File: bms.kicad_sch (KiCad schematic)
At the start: 62 parts, among them J1 Conn_01x13, U1 LMR51610, U2 STM32F103C8Tx, U3 MAX14920, U4 MAX11163, U5 MAX6126, Y1 8M

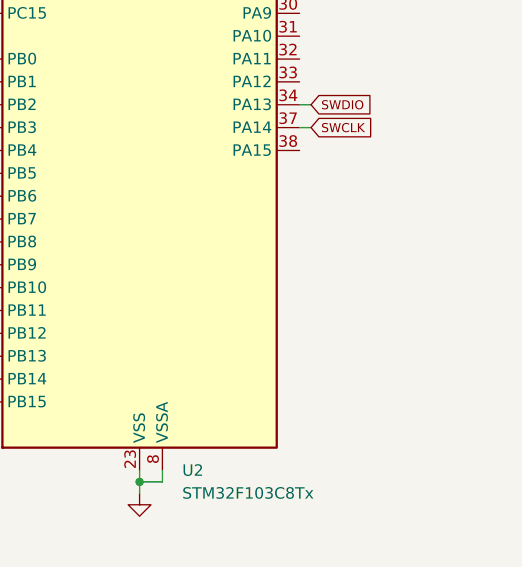
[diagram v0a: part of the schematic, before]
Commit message: schematic: Add SWD header
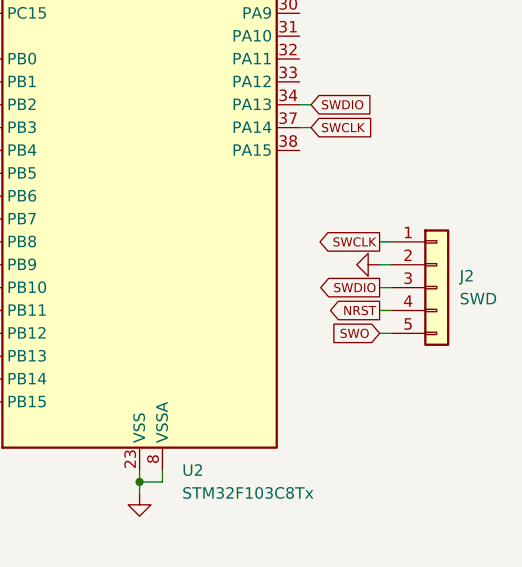
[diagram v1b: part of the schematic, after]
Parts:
- added J2: SWD, Connector_PinHeader_2.54mm:PinHeader_1x05_P2.54mm_Vertical, symbol Connector_Generic:Conn_01x05
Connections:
- net GND: now also J2.2 (Pin_2)
- net NRST: now also J2.4 (Pin_4)
- net SWCLK: now also J2.1 (Pin_1)
- net SWDIO: now also J2.3 (Pin_3)
- net SWO: now also J2.5 (Pin_5)

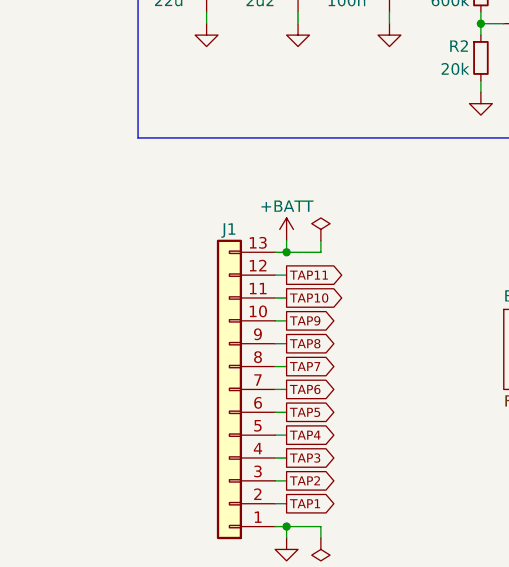
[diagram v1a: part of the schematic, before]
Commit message: schematic: Add mounting holes
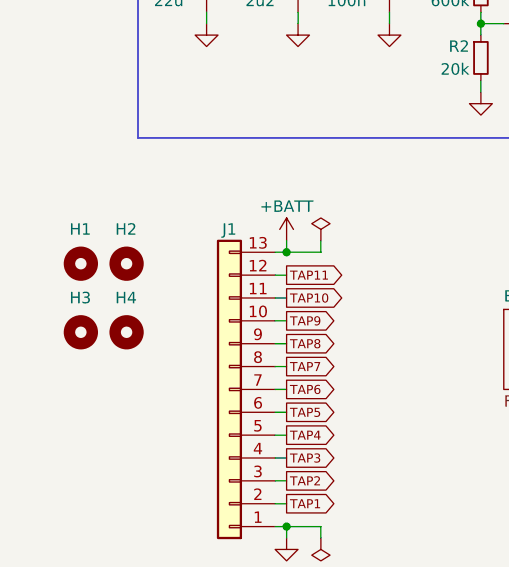
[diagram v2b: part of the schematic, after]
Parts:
- added H1, H2, H3, H4: MountingHole, MountingHole:MountingHole_3.2mm_M3, symbol Mechanical:MountingHole

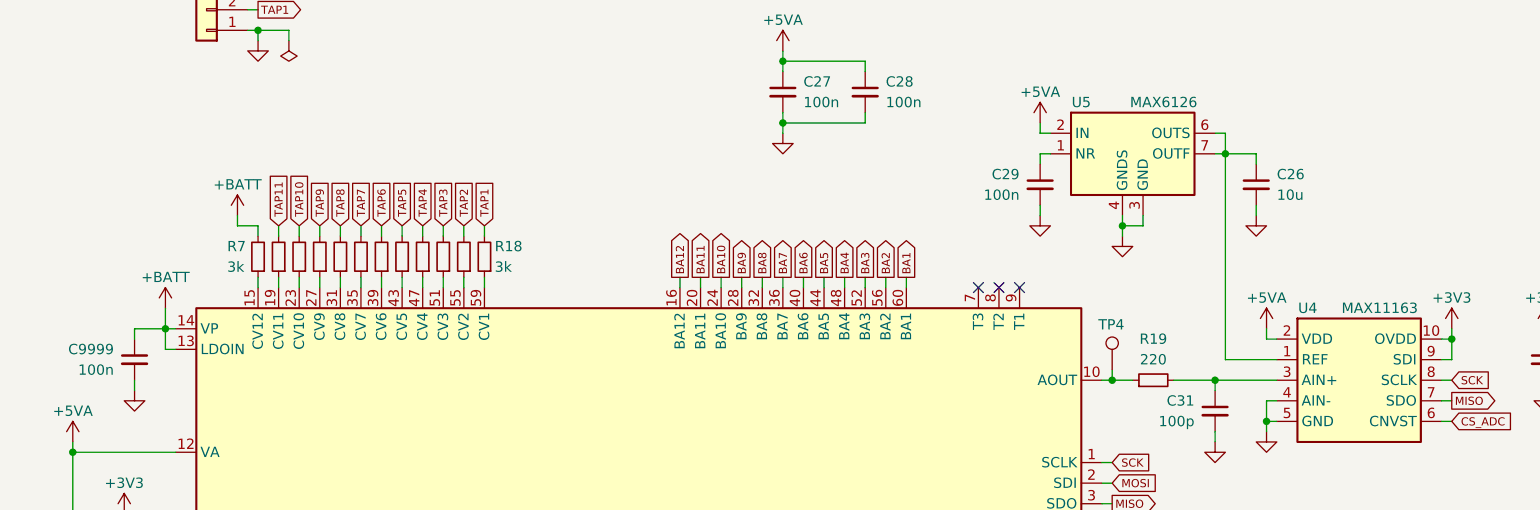
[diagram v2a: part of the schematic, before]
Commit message: schematic: Assign some more real components to passives
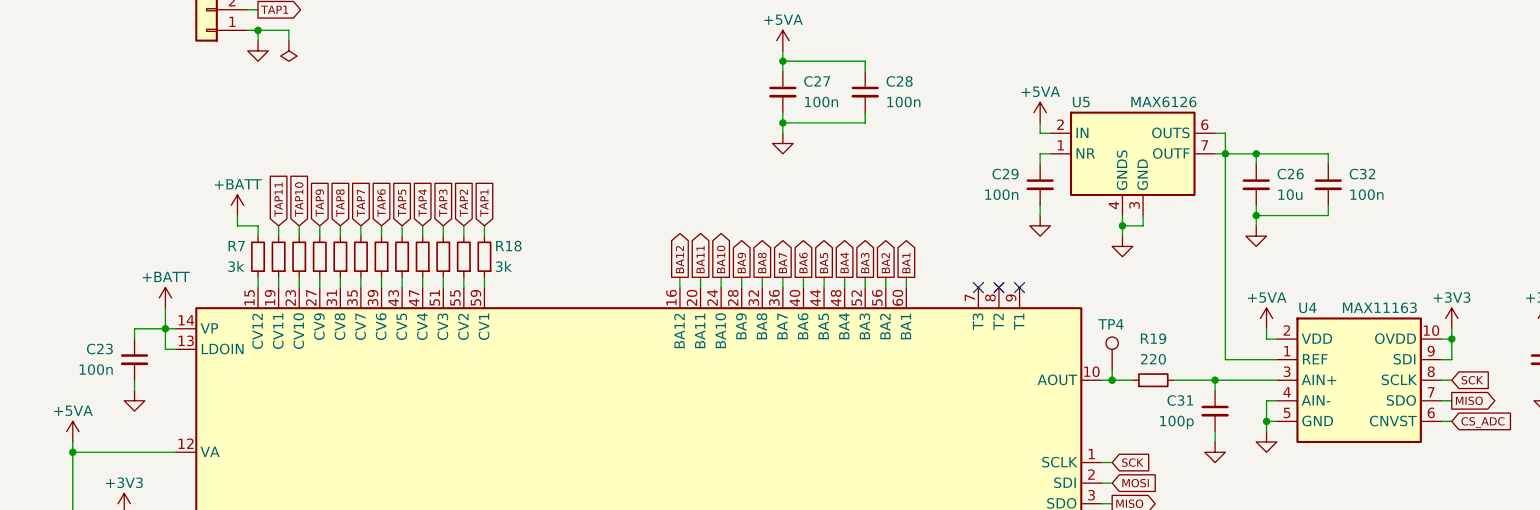
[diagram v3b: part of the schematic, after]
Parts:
- added C32: 100n, Capacitor_SMD:C_0603_1608Metric, symbol Device:C_Small
- C2: footprint (none) -> Capacitor_SMD:C_1210_3225Metric; Part Number (none) -> GRM32ER72A225KA35; Role (none) -> LMR51610 input decoupling
- C23: renamed from C9999; footprint (none) -> Capacitor_SMD:C_1206_3216Metric; Part Number (none) -> GRM31C5C2A104JA01L
- C26: footprint (none) -> Capacitor_SMD:C_1206_3216Metric; Part Number (none) -> GRM31CR71C106KA12L
- C3: footprint (none) -> Capacitor_SMD:C_1206_3216Metric; Part Number (none) -> GRM31C5C2A104JA01L; Role (none) -> LMR51610 input decoupling
- R10, R11, R12, R13, R14, R15, R16, R17, R18, R7, R8, R9: Part Number (none) -> 0603WAF3001T5E
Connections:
- net GND: now also C32.2
- net at C26.1, U4.1 (REF), U5.6 (OUTS)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: now also C32.1
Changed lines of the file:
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@@
 	)
 	(junction
+		(at 165.1 132.08)
+		(diameter 0)
+		(color 0 0 0 0)
+	)
+	(junction
 		(at 43.18 45.72)
 		(diameter 0)
@@
 	)
 	(junction
+		(at 165.1 124.46)
+		(diameter 0)
+		(color 0 0 0 0)
+	)
+	(junction
 		(at 33.02 45.72)
 		(diameter 0)
@@
 	(wire
 		(pts
+			(xy 173.99 125.73) (xy 173.99 124.46)
+		)
+		(stroke
+			(width 0)
+			(type default)
+		)
+	)
+	(wire
+		(pts
 			(xy 224.79 87.63) (xy 226.06 87.63)
 		)
@@
 	(wire
 		(pts
+			(xy 173.99 130.81) (xy 173.99 132.08)
+		)
+		(stroke
+			(width 0)
+			(type default)
+		)
+	)
+	(wire
+		(pts
 			(xy 138.43 121.92) (xy 139.7 121.92)
 		)
@@
 	(wire
 		(pts
+			(xy 165.1 132.08) (xy 173.99 132.08)
+		)
+		(stroke
+			(width 0)
+			(type default)
+		)
+	)
+	(wire
+		(pts
 			(xy 224.79 39.37) (xy 226.06 39.37)
 		)
@@
 	(wire
 		(pts
+			(xy 165.1 132.08) (xy 165.1 133.35)
+		)
+		(stroke
+			(width 0)
+			(type default)
+		)
+	)
+	(wire
+		(pts
 			(xy 41.91 109.22) (xy 41.91 110.49)
 		)
@@
 	(wire
 		(pts
+			(xy 173.99 124.46) (xy 165.1 124.46)
+		)
+		(stroke
+			(width 0)
+			(type default)
+		)
+	)
+	(wire
+		(pts
 			(xy 138.43 124.46) (xy 138.43 125.73)
 		)
@@
 			)
 		)
-		(property "Part Number" ""
+		(property "Part Number" "0603WAF3001T5E"
 			(at 46.99 137.16 0)
 			(effects
@@
 			)
 		)
-		(property "Part Number" ""
+		(property "Part Number" "0603WAF3001T5E"
 			(at 59.69 137.16 0)
 			(effects
@@
 			)
 		)
-		(property "Part Number" ""
+		(property "Part Number" "0603WAF3001T5E"
 			(at 49.53 137.16 0)
 			(effects
@@
 			)
 		)
-		(property "Part Number" ""
+		(property "Part Number" "0603WAF3001T5E"
 			(at 52.07 137.16 0)
 			(effects
@@
 			)
 		)
-		(property "Part Number" ""
+		(property "Part Number" "0603WAF3001T5E"
 			(at 54.61 137.16 0)
 			(effects
@@
 			)
 		)
-		(property "Part Number" ""
+		(property "Part Number" "0603WAF3001T5E"
 			(at 64.77 137.16 0)
 			(effects
@@
 			)
 		)
-		(property "Footprint" ""
+		(property "Footprint" "Capacitor_SMD:C_1206_3216Metric"
 			(at 165.1 128.27 0)
 			(effects
@@
 			)
 		)
+		(property "Part Number" "GRM31CR71C106KA12L"
+			(at 165.1 128.27 0)
+			(effects
+				(font
+					(size 1.27 1.27)
+				)
+				(hide yes)
+			)
+		)
 		(pin "1"
 		)
@@
 	)
 	(symbol
+		(lib_id "Device:C_Small")
+		(at 173.99 128.27 0)
+		(unit 1)
+		(exclude_from_sim no)
+		(in_bom yes)
+		(on_board yes)
+		(dnp no)
+		(fields_autoplaced yes)
+		(property "Reference" "C32"
+			(at 176.53 127.0062 0)
+			(effects
+				(font
+					(size 1.27 1.27)
+				)
+				(justify left)
+			)
+		)
+		(property "Value" "100n"
+			(at 176.53 129.5462 0)
+			(effects
+				(font
+					(size 1.27 1.27)
+				)
+				(justify left)
+			)
+		)
+		(property "Footprint" "Capacitor_SMD:C_0603_1608Metric"
+			(at 173.99 128.27 0)
+			(effects
+				(font
+					(size 1.27 1.27)
+				)
+				(hide yes)
+			)
+		)
+		(property "Datasheet" "~"
+			(at 173.99 128.27 0)
+			(effects
+				(font
+					(size 1.27 1.27)
+				)
+				(hide yes)
+			)
+		)
+		(property "Description" "Unpolarized capacitor, small symbol"
+			(at 173.99 128.27 0)
+			(effects
+				(font
+					(size 1.27 1.27)
+				)
+				(hide yes)
+			)
+		)
+		(property "Role" "MAX6126 output reference decoupling"
+			(at 173.99 128.27 0)
+			(effects
+				(font
+					(size 1.27 1.27)
+				)
+				(hide yes)
+			)
+		)
+		(pin "1"
+		)
+		(pin "2"
+		)
+		(instances
+			(project "bms"
+				(path "/ae4a7653-8e6d-4e05-b144-1e5e3b2092b7"
+					(reference "C32")
+					(unit 1)
+				)
+			)
+		)
+	)
+	(symbol
 		(lib_id "power:+BATT")
 		(at 30.48 143.51 0)
@@
 			)
 		)
-		(property "Part Number" ""
+		(property "Part Number" "0603WAF3001T5E"
 			(at 67.31 137.16 0)
 			(effects
@@
 	(symbol
 		(lib_id "power:GND")
-		(at 165.1 132.08 0)
+		(at 165.1 133.35 0)
 		(unit 1)
 		(exclude_from_sim no)
@@
 		(fields_autoplaced yes)
 		(property "Reference" "#PWR034"
-			(at 165.1 138.43 0)
+			(at 165.1 139.7 0)
 			(effects
 				(font
@@
 		)
 		(property "Value" "GND"
-			(at 165.1 137.16 0)
+			(at 165.1 138.43 0)
 			(effects
 				(font
@@
 		)
 		(property "Footprint" ""
-			(at 165.1 132.08 0)
+			(at 165.1 133.35 0)
 			(effects
 				(font
@@
 		)
 		(property "Datasheet" ""
-			(at 165.1 132.08 0)
+			(at 165.1 133.35 0)
 			(effects
 				(font
@@
 		)
 		(property "Description" "Power symbol creates a global label with name \"GND\" , ground"
-			(at 165.1 132.08 0)
+			(at 165.1 133.35 0)
 			(effects
 				(font
@@
 			)
 		)
-		(property "Footprint" ""
+		(property "Footprint" "Capacitor_SMD:C_1210_3225Metric"
 			(at 43.18 49.53 0)
 			(effects
@@
 			)
 		)
-		(property "Part Number" ""
+		(property "Part Number" "GRM32ER72A225KA35"
 			(at 43.18 49.53 0)
 			(effects
@@
 			)
 		)
-		(property "Role" ""
+		(property "Role" "LMR51610 input decoupling"
 			(at 43.18 49.53 0)
 			(effects
@@
 			)
 		)
-		(property "Part Number" ""
+		(property "Part Number" "0603WAF3001T5E"
 			(at 44.45 137.16 0)
 			(effects
@@
 			)
 		)
-		(property "Part Number" ""
+		(property "Part Number" "0603WAF3001T5E"
 			(at 57.15 137.16 0)
 			(effects
@@
 			)
 		)
-		(property "Footprint" ""
+		(property "Footprint" "Capacitor_SMD:C_1206_3216Metric"
 			(at 53.34 49.53 0)
 			(effects
@@
 			)
 		)
-		(property "Part Number" ""
+		(property "Part Number" "GRM31C5C2A104JA01L"
 			(at 53.34 49.53 0)
 			(effects
@@
 			)
 		)
-		(property "Role" ""
+		(property "Role" "LMR51610 input decoupling"
 			(at 53.34 49.53 0)
 			(effects
@@
 			)
 		)
-		(property "Part Number" ""
+		(property "Part Number" "0603WAF3001T5E"
 			(at 62.23 137.16 0)
 			(effects
@@
 			)
 		)
-		(property "Part Number" ""
+		(property "Part Number" "0603WAF3001T5E"
 			(at 41.91 137.16 0)
 			(effects
@@
 			)
 		)
-		(property "Part Number" ""
+		(property "Part Number" "0603WAF3001T5E"
 			(at 69.85 137.16 0)
 			(effects
@@
 		(on_board yes)
 		(dnp no)
-		(property "Reference" "C9999"
+		(property "Reference" "C23"
 			(at 24.13 148.5962 0)
 			(effects
@@
 			)
 		)
-		(property "Footprint" ""
+		(property "Footprint" "Capacitor_SMD:C_1206_3216Metric"
 			(at 26.67 149.86 0)
 			(effects
@@
 			)
 		)
-		(property "Part Number" ""
+		(property "Part Number" "GRM31C5C2A104JA01L"
 			(at 26.67 149.86 0)
 			(effects
@@
 			(project "bms"
 				(path "/ae4a7653-8e6d-4e05-b144-1e5e3b2092b7"
-					(reference "C9999")
+					(reference "C23")
 					(unit 1)
 				)

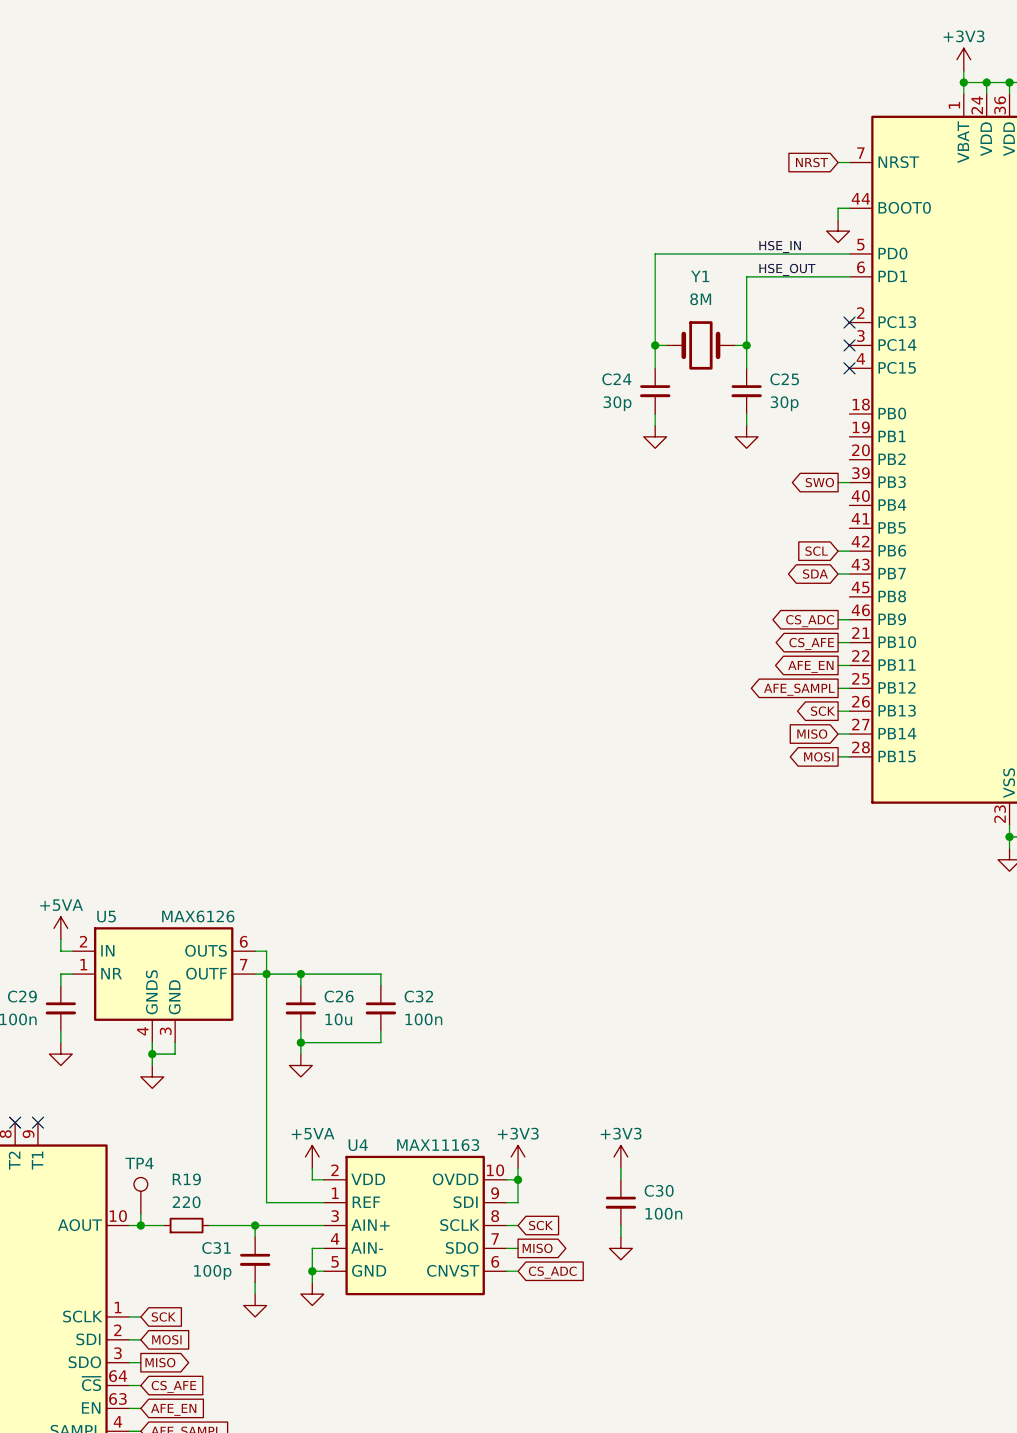
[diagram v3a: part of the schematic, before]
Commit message: schematic: Add isolated I2C
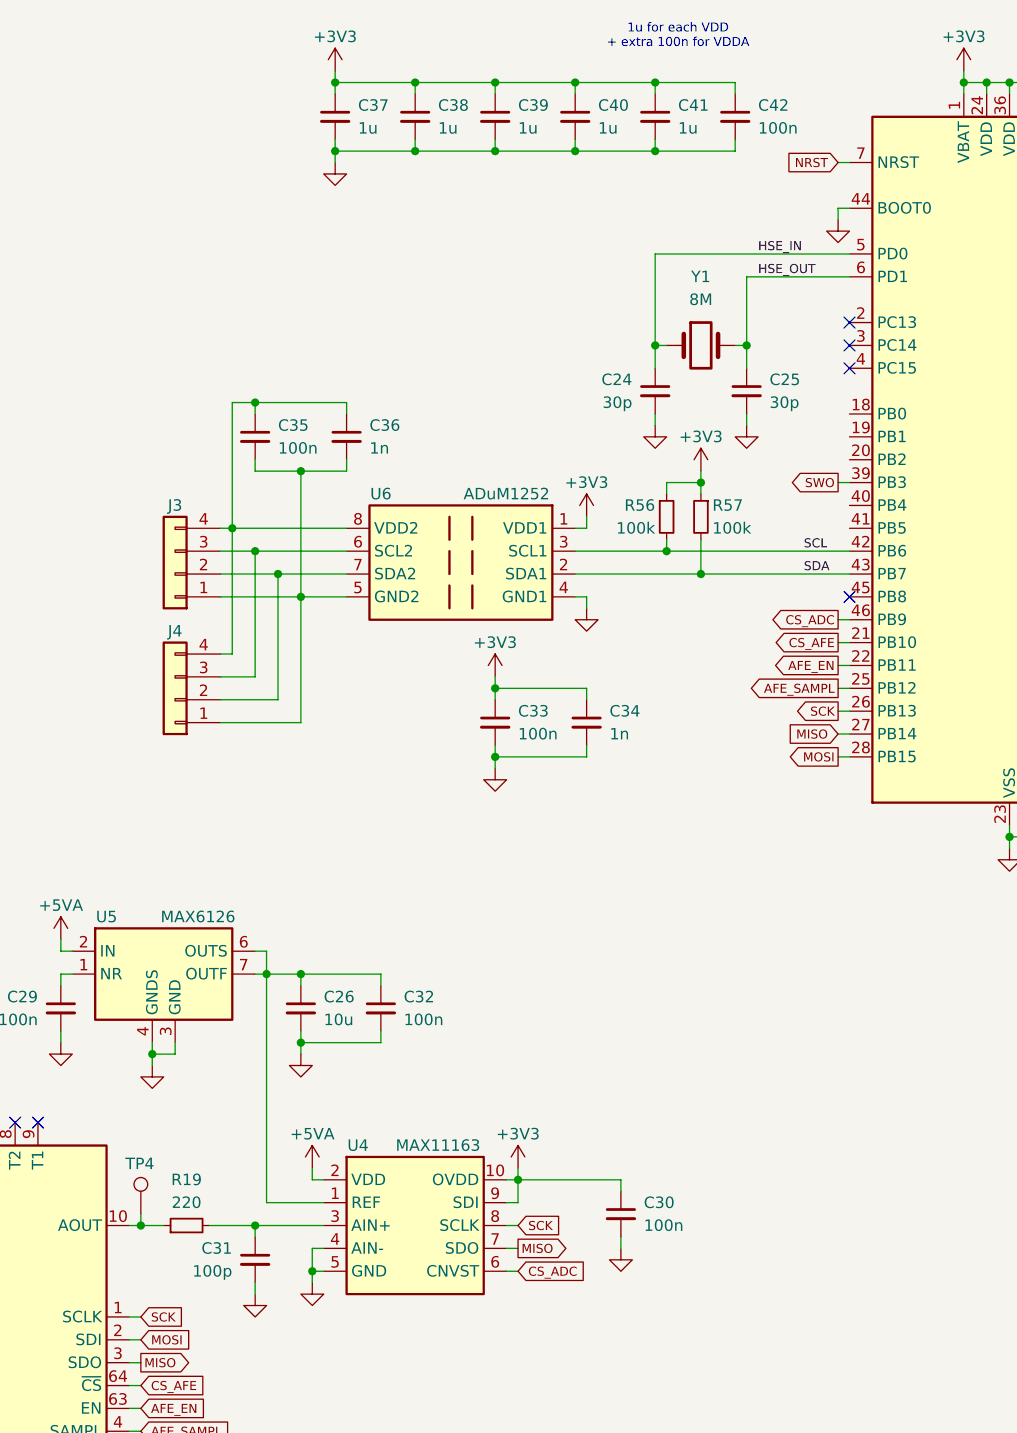
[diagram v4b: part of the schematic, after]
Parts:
- added C33, C35, C42: 100n, Capacitor_SMD:C_0603_1608Metric, symbol Device:C_Small
- added C34, C36: 1n, Capacitor_SMD:C_0603_1608Metric, symbol Device:C_Small
- added C37, C38, C39, C40, C41: 1u, Capacitor_SMD:C_0603_1608Metric, symbol Device:C_Small
- added J3: I2C_IN, symbol Connector_Generic:Conn_01x04
- added J4: I2C_OUT, symbol Connector_Generic:Conn_01x04
- added R56, R57: 100k, Resistor_SMD:R_0603_1608Metric, symbol Device:R_Small
- added U6: ADuM1252, Package_SO:MSOP-8_3x3mm_P0.65mm, symbol bms:ADuM1252
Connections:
- net +3V3: now also C33.1, C34.1, C37.1, C38.1, C39.1, C40.1, C41.1, C42.1, R56.1, R57.1, U6.1 (VDD1)
- net GND: now also C33.2, C34.2, C37.2, C38.2, C39.2, C40.2, C41.2, C42.2, U6.4 (GND1)
- net SCL: now also R56.2, U6.3 (SCL1)
- net SDA: now also R57.2, U6.2 (SDA1)
- new net: C35.2, C36.2, J3.1 (Pin_1), J4.1 (Pin_1), U6.5 (GND2)
- new net: J3.3 (Pin_3), J4.3 (Pin_3), U6.6 (SCL2)
- new net: J3.2 (Pin_2), J4.2 (Pin_2), U6.7 (SDA2)
- new net: C35.1, C36.1, J3.4 (Pin_4), J4.4 (Pin_4), U6.8 (VDD2)
- no-connect marks 6 -> 7
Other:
- note added: "1u for each VDD + extra 100n for VDDA"
- moved on the sheet: C30
